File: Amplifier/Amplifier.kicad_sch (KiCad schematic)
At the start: 28 parts, among them J1 Conn_01x01_Pin, J10 Conn_01x01_Pin, J11 Conn_01x01_Pin, J2 Conn_01x01_Pin, J9 Conn_01x10, Q1 JFE2140D, Q2 Q_NJFET_DSG, U16 LTC6268xS8, U2 LMP7721

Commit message: Signed-off-by: lokimetasmith <lokimail@gmail.com>
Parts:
- J1, J10, J11, J2: footprint footprints:Electrode_Guard -> footprints:Electrode_Guard_Shield; symbol Connector:Conn_01x01_Pin -> Connector:Conn_Coaxial_Small
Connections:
- net GNDA: now also J10.2 (Ext), J11.2 (Ext), J2.2 (Ext)
- net GUARD: now also J1.2 (Ext)

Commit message: Signed-off-by: lokimetasmith <lokimail@gmail.com>
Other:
- moved on the sheet: C19, J2, R6

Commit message: Signed-off-by: lokimetasmith <lokimail@gmail.com>
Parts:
- added J3, J4, J5, J6: Conn_Shielded_Pair, symbol Connector:Conn_Shielded_Pair
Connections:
- net >PORE_AMP: now also J6.2 (In2)
- net GNDA: now also J4.2 (In2), J5.2 (In2), J6.1 (In1)
- net SHIELD_AMP: now also J3.1 (In1), J3.3 (Ext), J4.3 (Ext), J5.3 (Ext), J6.3 (Ext)
- net VDDA: now also J4.1 (In1)
- net VSSA: now also J5.1 (In1)
- net Vbias_AMP: now also J3.2 (In2)
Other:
- moved on the sheet: Q1A, Q1B, Q1C, Q2

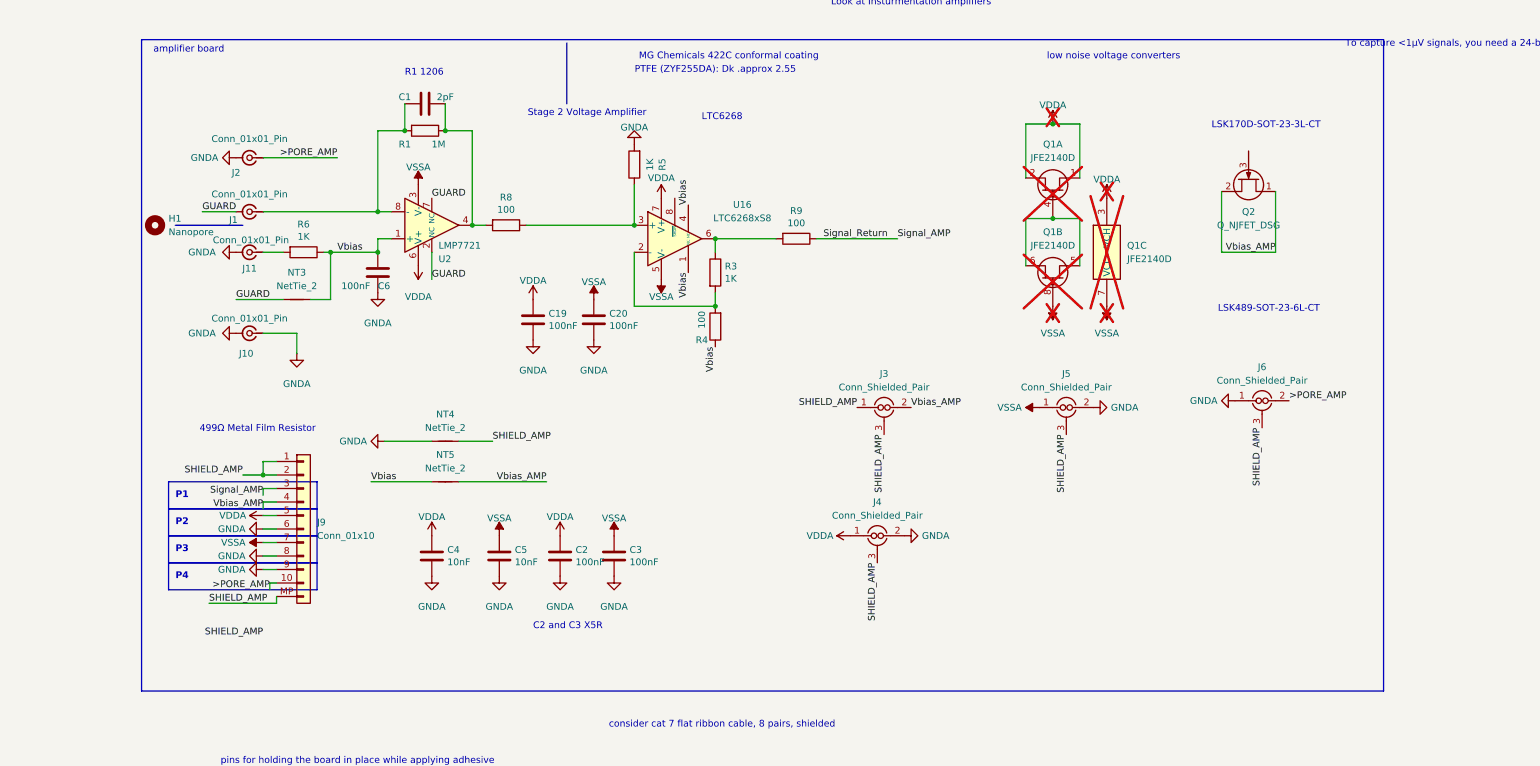
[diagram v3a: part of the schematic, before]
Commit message: feat(amplifier): digitize frontend with AD40xx ADC, ADA4940 driver, LP5907 LDO, 6-pin pogo header, and interleaved ribbon pinout
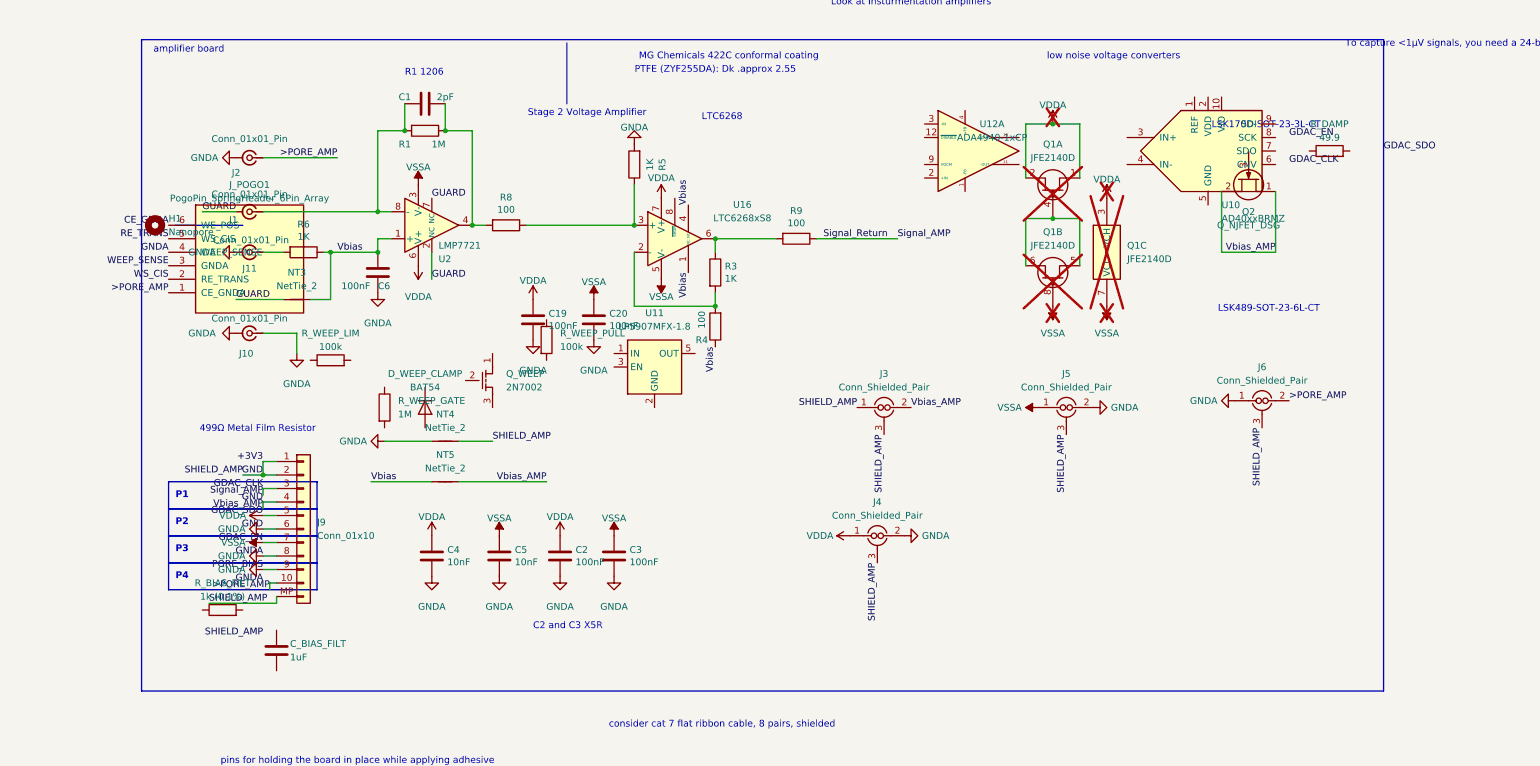
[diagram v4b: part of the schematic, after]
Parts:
- added C_BIAS_FILT: 1uF, Capacitor_SMD:C_0402_1005Metric, symbol Device:C
- added D_WEEP_CLAMP: BAT54, Diode_SMD:D_SOD-323, symbol Diode:BAT54
- added J_POGO1: PogoPin_SpringHeader_6Pin_Array, footprints:PogoPin_SpringHeader_6Pin_Array, symbol Amplifier:PogoPin_SpringHeader_6Pin_Array
- added Q_WEEP: 2N7002, Package_TO_SOT_SMD:SOT-23, symbol Transistor_FET:2N7002
- added R_BIAS_FILT: 1k (0.1%), Resistor_SMD:R_0402_1005Metric, symbol Device:R
- added R_DAMP: 49.9, Resistor_SMD:R_0402_1005Metric, symbol Device:R
- added R_WEEP_GATE: 1M, Resistor_SMD:R_0402_1005Metric, symbol Device:R
- added R_WEEP_LIM, R_WEEP_PULL: 100k, Resistor_SMD:R_0402_1005Metric, symbol Device:R
- added U10: AD40xxBRMZ, Package_SO:MSOP-10_3x3mm_P0.5mm, symbol Analog_ADC:AD40xxBRMZ
- added U11: LP5907MFX-1.8, Package_TO_SOT_SMD:SOT-23-5, symbol Regulator_Linear:LP5907MFX-1.8
- added U12: ADA4940-1xCP, Package_CSP:LFCSP-16-1EP_3x3mm_P0.5mm_EP1.3x1.3mm_ThermalVias, symbol Amplifier_Difference:ADA4940-1xCP
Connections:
- net SHIELD_AMP is gone; now on net GNDA: J3.1 (In1), J3.3 (Ext), J4.3 (Ext), J5.3 (Ext), J6.3 (Ext), J9.1 (Pin_1), J9.2 (Pin_2), J9.MP (Pin_11), NT4.2
- net Vbias_AMP is gone; now on net GNDA: J3.2 (In2), J9.4 (Pin_4), NT5.2, Q2.1 (D), Q2.2 (S)
- net >PORE_AMP: now also J_POGO1.1 (CE_GNDA)
- net GNDA: now also J_POGO1.4 (WEEP_SENSE)
- net Signal_AMP renamed GDAC_CLK
- new net CE_GNDA: J_POGO1.6 (WE_POS)
- new net RE_TRANS: J_POGO1.5 (WS_CIS)
- new net WEEP_SENSE: J_POGO1.3 (GNDA)
- new net WS_CIS: J_POGO1.2 (RE_TRANS)

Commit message: Signed-off-by: lokimetasmith <lokimail@gmail.com>
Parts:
- removed C2: 100nF, Capacitor_SMD:C_0805_2012Metric, symbol Device:C
- removed C3: 100nF, Capacitor_SMD:C_0402_1005Metric, symbol Device:C
- removed C4, C5: 10nF, Capacitor_SMD:C_0402_1005Metric, symbol Device:C
- removed C_BIAS_FILT: 1uF, Capacitor_SMD:C_0402_1005Metric, symbol Device:C
- removed D_WEEP_CLAMP: BAT54, Diode_SMD:D_SOD-323, symbol Diode:BAT54
- removed H1: Nanopore, footprints:Nanopore holder_recessed, symbol Mechanical:MountingHole
- removed J1, J10, J11, J2: Conn_01x01_Pin, footprints:Electrode_Guard_Shield, symbol Connector:Conn_Coaxial_Small
- removed J3, J4, J5, J6: Conn_Shielded_Pair, symbol Connector:Conn_Shielded_Pair
- removed J9: Conn_01x10, Connector_JST:JST_SH_SM10B-SRSS-TB_1x10-1MP_P1.00mm_Horizontal, symbol MR1:Conn_01x11_MP
- removed Q_WEEP: 2N7002, Package_TO_SOT_SMD:SOT-23, symbol Transistor_FET:2N7002
- removed R9: 100, Resistor_SMD:R_0805_2012Metric, symbol Device:R
- removed R_BIAS_FILT: 1k (0.1%), Resistor_SMD:R_0402_1005Metric, symbol Device:R
- removed R_WEEP_GATE: 1M, Resistor_SMD:R_0402_1005Metric, symbol Device:R
- removed R_WEEP_LIM, R_WEEP_PULL: 100k, Resistor_SMD:R_0402_1005Metric, symbol Device:R
- removed U10: AD40xxBRMZ, Package_SO:MSOP-10_3x3mm_P0.5mm, symbol Analog_ADC:AD40xxBRMZ
- removed U11: LP5907MFX-1.8, Package_TO_SOT_SMD:SOT-23-5, symbol Regulator_Linear:LP5907MFX-1.8
- removed U12: ADA4940-1xCP, Package_CSP:LFCSP-16-1EP_3x3mm_P0.5mm_EP1.3x1.3mm_ThermalVias, symbol Amplifier_Difference:ADA4940-1xCP
- added C10, C12, C31, C32, C33, C39: 100nF, Capacitor_SMD:C_0402_1005Metric, symbol Device:C
- added C11: 4.7u, Capacitor_SMD:C_0402_1005Metric, symbol Device:C_Small
- added C29, C30: 10pF, Capacitor_SMD:C_0402_1005Metric, symbol Device:C
- added C35: 10u, Capacitor_SMD:C_0402_1005Metric, symbol Device:C_Small
- added C41: 1nF, Capacitor_SMD:C_0402_1005Metric, symbol Device:C_Small
- added C7, C8: 10nF, Capacitor_SMD:C_0402_1005Metric, symbol Device:C
- added D82: MBR0540, Diode_SMD:D_SOD-123, symbol Diode:MBR0540
- added J7: Conn_01x14_MountingPin, symbol Connector_Generic_MountingPin:Conn_01x14_MountingPin
- added NT7, NT8: NetTie_2, NetTie:NetTie-2_SMD_Pad0.5mm, symbol Device:NetTie_2
- added Q3: 2N7002, Package_TO_SOT_SMD:SOT-23, symbol Transistor_FET:2N7002
- added R14, R15: 100k, symbol Device:R
- added R16: 1M, Resistor_SMD:R_0402_1005Metric, symbol Device:R
- added R27, R41: 27, Resistor_SMD:R_0402_1005Metric, symbol Device:R_Small_US
- added R28, R29, R30, R31: 49.9, Resistor_SMD:R_0402_1005Metric, symbol Device:R_Small_US
- added R43, R44, R45, R46: 499 (0.1%), Resistor_SMD:R_0402_1005Metric, symbol Device:R
- added U13: AD40xxBRMZ, Package_SO:MSOP-10_3x3mm_P0.5mm, symbol Analog_ADC:AD40xxBRMZ
- added U14: LP5907MFX-1.8, Package_TO_SOT_SMD:SOT-23-5, symbol Regulator_Linear:LP5907MFX-1.8
- added U6: ADA4940-1xCP, Package_CSP:LFCSP-16-1EP_3x3mm_P0.5mm_EP1.3x1.3mm_ThermalVias, symbol Amplifier_Difference:ADA4940-1xCP
- J_POGO1: symbol Amplifier:PogoPin_SpringHeader_6Pin_Array -> MR1:PogoPin_SpringHeader_6Pin_Array
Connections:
- net WEEP_SENSE is gone; now on net GNDA: J_POGO1.3 (GNDA)
- net >PORE_AMP: now also J_POGO1.6 (WE_POS), J7.14 (Pin_14); no longer J_POGO1.1 (CE_GNDA)
- net CE_GNDA: now also J_POGO1.1 (CE_GNDA), NT8.1; no longer J_POGO1.6 (WE_POS)
- net GDAC_CLK: now also R31.1, U13.8 (SCK)
- net GNDA: now also C10.2, C12.2, C29.1, C30.2, C31.2, C32.2, C33.2, C35.2, C39.2, C7.2, C8.2, D82.2 (A), J7.11 (Pin_11), J7.13 (Pin_13), J7.9 (Pin_9), NT8.2, Q3.2 (S), R43.1, U13.5 (GND), U6.17 (EP), U6.9 (VOCM); no longer J_POGO1.4 (WEEP_SENSE), NT4.2, NT5.2, Q2.1 (D), Q2.2 (S)
- net RE_TRANS: now also J_POGO1.2 (RE_TRANS), R6.2; no longer J_POGO1.5 (WS_CIS)
- net VDDA: now also C10.1, C31.1, C7.1, J7.10 (Pin_10), U6.5 (+Vs), U6.6 (+Vs), U6.7 (+Vs), U6.8 (+Vs)
- net VSSA: now also C12.1, C32.1, C8.1, J7.12 (Pin_12), U6.13 (-Vs), U6.14 (-Vs), U6.15 (-Vs), U6.16 (-Vs)
- net Vbias: now also C35.1, U13.1 (REF)
- net WS_CIS: now also C1.2, J_POGO1.5 (WS_CIS), R1.2, U2.8 (-); no longer J_POGO1.2 (RE_TRANS)
- net Signal_AMP: now reaches R3.1, U16.6
- net Signal_AMP: now also R45.1
- net Virtual_Ground: now reaches R3.2, R4.2, U16.2 (-)
- new net: C30.1, C41.2, R41.2, U13.4 (IN-)
- new net: J7.7 (Pin_7), R30.2
- new net: R43.2, R44.1, U6.3 (-IN)
- new net: R44.2, U6.4 (+FB)
- new net: C29.2, C41.1, R27.2, U13.3 (IN+)
- new net: C39.1, NT7.1
- new net: Q3.1 (G), R16.2
- new net: R41.1, U6.11 (-OUT)
- new net: J7.3 (Pin_3), R31.2
- new net: J7.5 (Pin_5), R28.2
- new net: J7.6 (Pin_6), R29.2
- new net: R45.2, R46.2, U6.2 (+IN)
- new net: R27.1, U6.10 (+OUT)
- new net: R46.1, U6.1 (-FB)
- new net +1V8: C11.1, U13.2 (VDD), U14.5 (OUT)
- new net +3V3: C33.1, J7.1 (Pin_1), R14.1, U13.10 (VIO), U14.1 (IN)
- new net GDAC_EN: R30.1, U13.6 (CNV)
- new net GDAC_SDI: R29.1, U13.9 (SDI)
- new net GDAC_SDO: R28.1, U13.7 (SDO)
- new net GND: C11.2, J7.2 (Pin_2), J7.4 (Pin_4), J7.8 (Pin_8), U14.2 (GND)
- new net R_WEEP_GATE: D82.1 (K), R15.2, R16.1
- new net R_WEEP_LIM: J_POGO1.4 (WEEP_SENSE), R15.1
- new net R_WEEP_PULL: Q3.3 (D), R14.2, U14.3 (EN)
- new net SHIELD: NT7.2
- new net SHIELD_AMP: J7.MP (MountPin), NT4.2
- new net Vbias_AMP: NT5.2, Q2.1 (D), Q2.2 (S)
- no-connect marks 0 -> 2
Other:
- note added: "RF-damping capacitor"
- note added: "R_DAMP"
- note added: "Stage 1: Transimpedance Amp"
- note added: "we need to play back a waveform"
- moved on the sheet: C1, C19, C20, C6, J_POGO1, NT3, NT4, NT5, Q1A, Q1B, Q1C, Q2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

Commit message: updated amplifier
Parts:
- R14, R15: footprint (none) -> Resistor_SMD:R_0402_1005Metric
- renumbered R_DAMP to R_DAMP1

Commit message: lots of layout changes.
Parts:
- removed Q1: JFE2140D, Package_SO:SOIC-8_3.9x4.9mm_P1.27mm, symbol Transistor_FET:JFE2140D
- removed Q2: Q_NJFET_DSG, symbol Device:Q_NJFET_DSG
- removed R_DAMP1: 49.9, Resistor_SMD:R_0402_1005Metric, symbol Device:R
- added C9: 100nF, Capacitor_SMD:C_0805_2012Metric, symbol Device:C
- added H1, H2, H3, H4: FluidHole, MountingHole:MountingHole_2.1mm, symbol Mechanical:MountingHole
- J7: footprint (none) -> Connector_FFC-FPC:Amphenol_F32R-1A7x1-11014_1x14-1MP_P0.5mm_Horizontal
- J_POGO1: footprint footprints:PogoPin_SpringHeader_6Pin_Array -> footprints:PogoPin_Target_6Pin_Distributed
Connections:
- net GDAC_EN: now also R29.1; no longer R30.1
- net GDAC_SDI: now also R30.1; no longer R29.1
- net R_WEEP_LIM: now also J_POGO1.5 (WS_CIS); no longer J_POGO1.4 (WEEP_SENSE)
- net Signal_AMP: now also C9.1
- net VDDA: now also J7.12 (Pin_12); no longer J7.10 (Pin_10)
- net VSSA: now also J7.10 (Pin_10); no longer J7.12 (Pin_12)
- net Virtual_Ground: now also C9.2
- net WS_CIS: now also J_POGO1.4 (WEEP_SENSE); no longer J_POGO1.5 (WS_CIS)
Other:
- note removed: "LSK170D-SOT-23-3L-CT"
- note removed: "LSK489-SOT-23-6L-CT"
